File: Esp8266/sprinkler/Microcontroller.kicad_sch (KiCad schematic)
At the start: 0 parts

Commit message: Sprinklers
Added RTC and valver drivers modules for the Sprinklers
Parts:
- added J4: DF9B-19P-1V32, User_Footprint:CON9_1X19_MDL_DF9_HIR, symbol _Connectors:DF9B-19P-1V32
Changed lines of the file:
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@@
 	(generator_version "9.0")
 	(paper "A4")
+	(symbol
+		(lib_id "_Connectors:DF9B-19P-1V32")
+		(at 134.62 63.5 0)
+		(unit 1)
+		(exclude_from_sim no)
+		(in_bom yes)
+		(on_board yes)
+		(dnp no)
+		(fields_autoplaced yes)
+		(property "Reference" "J4"
+			(at 148.59 84.4549 0)
+			(effects
+				(font
+					(size 1.524 1.524)
+				)
+				(justify left)
+			)
+		)
+		(property "Value" "DF9B-19P-1V32"
+			(at 148.59 88.2649 0)
+			(effects
+				(font
+					(size 1.524 1.524)
+				)
+				(justify left)
+			)
+		)
+		(property "Footprint" "User_Footprint:CON9_1X19_MDL_DF9_HIR"
+			(at 134.62 63.5 0)
+			(effects
+				(font
+					(size 1.27 1.27)
+					(italic yes)
+				)
+				(hide yes)
+			)
+		)
+		(property "Datasheet" "DF9B-19P-1V32"
+			(at 134.62 63.5 0)
+			(effects
+				(font
+					(size 1.27 1.27)
+					(italic yes)
+				)
+				(hide yes)
+			)
+		)
+		(property "Description" ""
+			(at 134.62 63.5 0)
+			(effects
+				(font
+					(size 1.27 1.27)
+				)
+				(hide yes)
+			)
+		)
+		(pin "18"
+		)
+		(pin "19"
+		)
+		(pin "17"
+		)
+		(pin "5"
+		)
+		(pin "4"
+		)
+		(pin "6"
+		)
+		(pin "13"
+		)
+		(pin "14"
+		)
+		(pin "8"
+		)
+		(pin "3"
+		)
+		(pin "2"
+		)
+		(pin "1"
+		)
+		(pin "15"
+		)
+		(pin "12"
+		)
+		(pin "16"
+		)
+		(pin "7"
+		)
+		(pin "9"
+		)
+		(pin "11"
+		)
+		(pin "10"
+		)
+		(instances
+			(project ""
+				(path "/00ed8740-45a2-4b9d-9104-9548b81da339/8377aa62-8d99-48c6-8d5e-0da5edecd305"
+					(reference "J4")
+					(unit 1)
+				)
+			)
+		)
+	)
 )

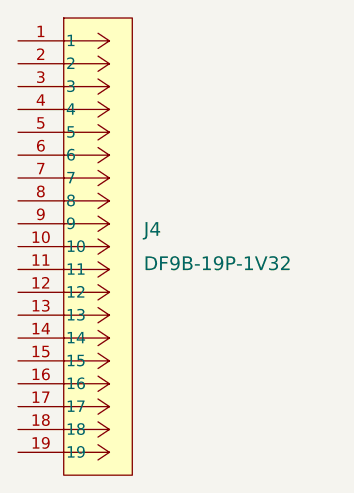
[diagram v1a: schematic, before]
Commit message: Transistor changes
Changed all Bjt transistors to Mosfets
Assign footprints
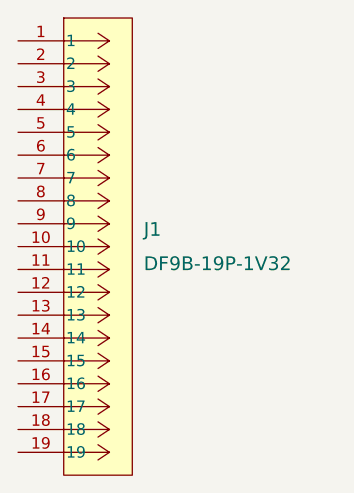
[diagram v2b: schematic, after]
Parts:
- renumbered J4 to J1
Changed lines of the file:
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@@
 		(dnp no)
 		(fields_autoplaced yes)
-		(property "Reference" "J4"
+		(property "Reference" "J1"
 			(at 148.59 84.4549 0)
 			(effects
@@
 			(project ""
 				(path "/00ed8740-45a2-4b9d-9104-9548b81da339/8377aa62-8d99-48c6-8d5e-0da5edecd305"
-					(reference "J4")
+					(reference "J1")
 					(unit 1)
 				)

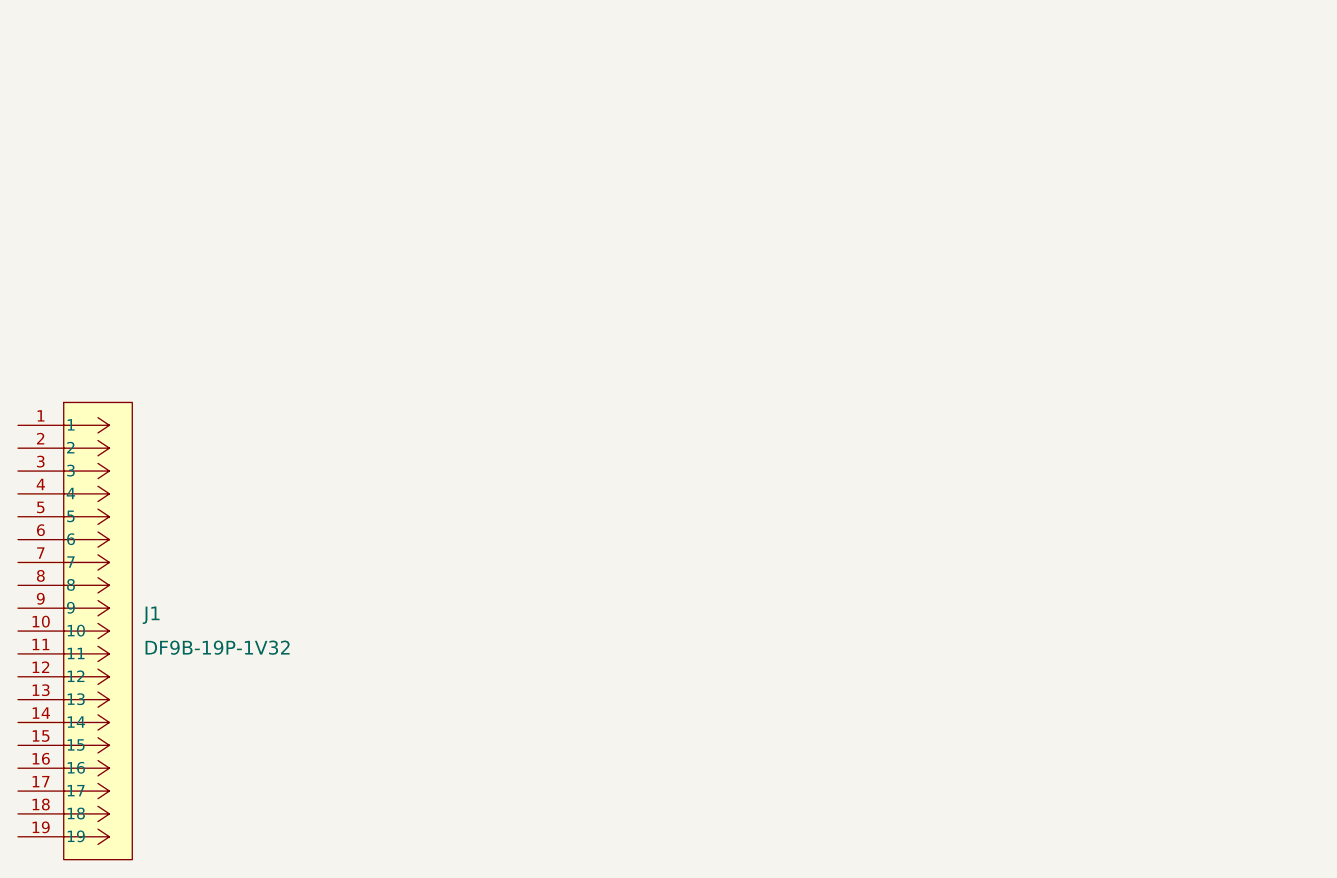
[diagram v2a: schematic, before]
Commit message: Update connections
Connect Micro controller inputs and outputs
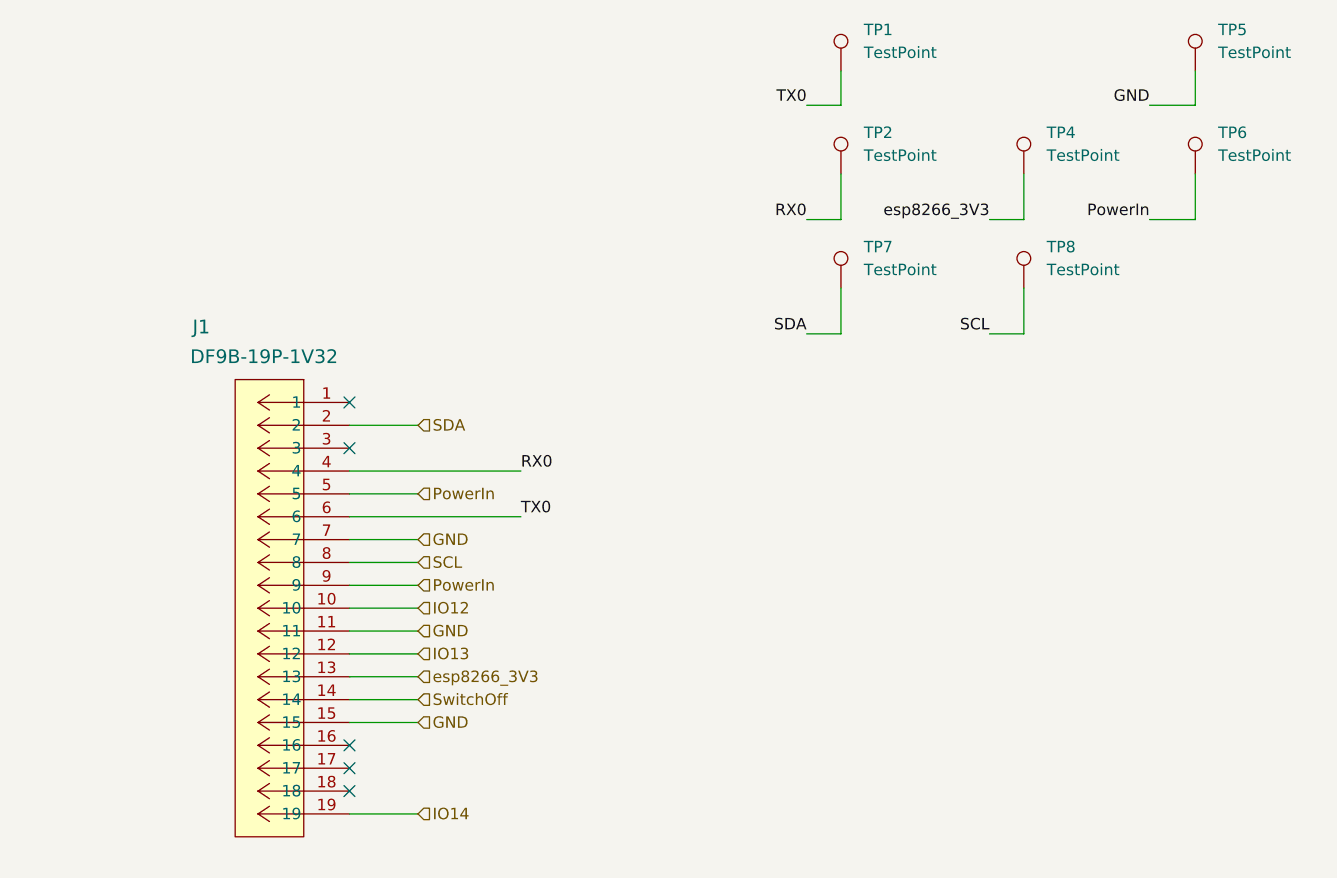
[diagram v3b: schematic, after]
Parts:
- added TP1, TP2, TP4, TP5, TP6, TP7, TP8: TestPoint, TestPoint:TestPoint_Pad_1.0x1.0mm, symbol Connector:TestPoint
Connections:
- net IO12: now reaches J1.10
- net GND: now reaches J1.11
- net GND: now also J1.15, J1.7, TP5.1
- net IO13: now reaches J1.12
- net esp8266_3V3: now reaches J1.13
- net esp8266_3V3: now also TP4.1
- net SwitchOff: now reaches J1.14
- net IO14: now reaches J1.19
- net SDA: now reaches J1.2
- net SDA: now also TP7.1
- net RX0: now reaches J1.4
- net RX0: now also TP2.1
- net PowerIn: now reaches J1.5
- net PowerIn: now also J1.9, TP6.1
- net TX0: now reaches J1.6
- net TX0: now also TP1.1
- net SCL: now reaches J1.8
- net SCL: now also TP8.1
- no-connect marks 0 -> 5
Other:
- moved on the sheet: J1

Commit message: pcb
First component layout (need to verify ESP8266 board size for fitment)
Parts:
- renumbered J1 to J3, TP7 to TP3, TP8 to TP5, TP5 to TP6, TP6 to TP7
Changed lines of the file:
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@@
 		(on_board yes)
 		(dnp no)
-		(property "Reference" "J1"
+		(property "Reference" "J3"
 			(at 155.956 52.578 0)
 			(effects
@@
 			(project ""
 				(path "/00ed8740-45a2-4b9d-9104-9548b81da339/8377aa62-8d99-48c6-8d5e-0da5edecd305"
-					(reference "J1")
+					(reference "J3")
 					(unit 1)
 				)
@@
 		(dnp no)
 		(fields_autoplaced yes)
-		(property "Reference" "TP8"
+		(property "Reference" "TP5"
 			(at 248.92 43.688 0)
 			(effects
@@
 			(project "sprinkler"
 				(path "/00ed8740-45a2-4b9d-9104-9548b81da339/8377aa62-8d99-48c6-8d5e-0da5edecd305"
-					(reference "TP8")
+					(reference "TP5")
 					(unit 1)
 				)
@@
 		(dnp no)
 		(fields_autoplaced yes)
-		(property "Reference" "TP5"
+		(property "Reference" "TP6"
 			(at 267.97 19.558 0)
 			(effects
@@
 			(project ""
 				(path "/00ed8740-45a2-4b9d-9104-9548b81da339/8377aa62-8d99-48c6-8d5e-0da5edecd305"
-					(reference "TP5")
+					(reference "TP6")
 					(unit 1)
 				)
@@
 		(dnp no)
 		(fields_autoplaced yes)
-		(property "Reference" "TP6"
+		(property "Reference" "TP7"
 			(at 267.97 30.988 0)
 			(effects
@@
 			(project ""
 				(path "/00ed8740-45a2-4b9d-9104-9548b81da339/8377aa62-8d99-48c6-8d5e-0da5edecd305"
-					(reference "TP6")
+					(reference "TP7")
 					(unit 1)
 				)
@@
 		(dnp no)
 		(fields_autoplaced yes)
-		(property "Reference" "TP7"
+		(property "Reference" "TP3"
 			(at 228.6 43.688 0)
 			(effects
@@
 			(project "sprinkler"
 				(path "/00ed8740-45a2-4b9d-9104-9548b81da339/8377aa62-8d99-48c6-8d5e-0da5edecd305"
-					(reference "TP7")
-					(unit 1)
-				)
+					(reference "TP3")
+					(unit 1)
+				)

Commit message: Traces
Layout traces for the PCB
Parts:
- removed TP1, TP2, TP3, TP4, TP5: TestPoint, TestPoint:TestPoint_Pad_1.0x1.0mm, symbol Connector:TestPoint
